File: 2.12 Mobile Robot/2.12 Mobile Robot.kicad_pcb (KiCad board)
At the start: 4 copper layers, 176 x 56 mm, 82 parts, among them J1 Motor Control B, J10 Encoder 1, J11 Encoder 2, J12 Encoder 3, J13 Encoder 4, J2 Motor Control A, J3 GND, J4 Motor Power A, J5 Battery Power, J6 Motor Power B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

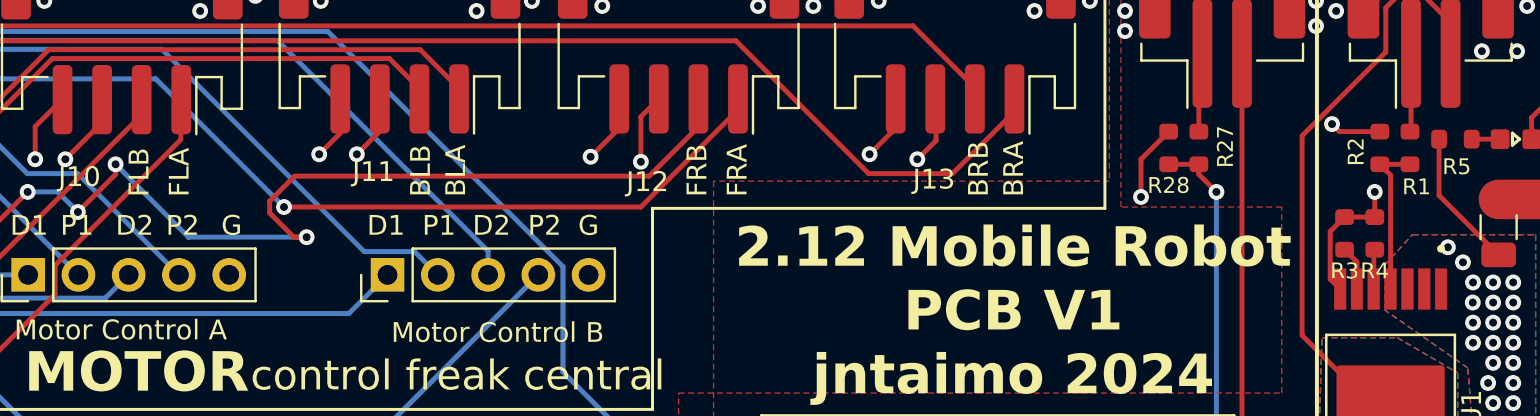
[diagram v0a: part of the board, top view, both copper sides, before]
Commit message: fixed silkscreen error
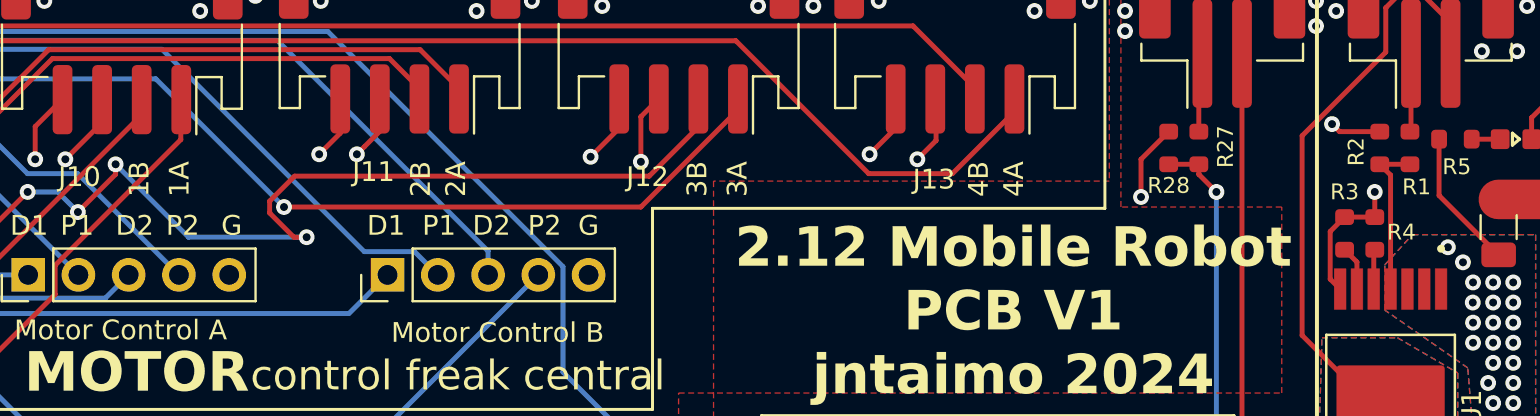
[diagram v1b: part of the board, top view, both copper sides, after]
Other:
- board text added: "1A"
- board text added: "1B"
- board text added: "2A"
- board text added: "2B"
- board text added: "3A"
- board text added: "3B"
- board text added: "4A"
- board text added: "4B"
- board text removed: "BLA"
- board text removed: "BLB"
- board text removed: "BRA"
- board text removed: "BRB"
- board text removed: "FLA"
- board text removed: "FLB"
- board text removed: "FRA"
- board text removed: "FRB"
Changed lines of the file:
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@@
   (title_block
     (title "2.12 Mobile Robot PCB")
-    (date "2024-02-17")
+    (date "2024-02-24")
     (rev "V1")
     (company "MIT jntaimo")
@@
     (property "ki_description" "1% 1 10W Thick Film Resistors 75V   100ppm    -55    155   15k   0603 Chip Resistor - Surface Mount ROHS")
     (attr smd)
-    (fp_text reference "R3" (at -1.9 0 180) (layer "F.SilkS")
+    (fp_text reference "R3" (at 2.095 0 180) (layer "F.SilkS")
         (effects (font (size 0.8 0.8) (thickness 0.15)))
     )
@@
     (property "ki_keywords" "connector")
     (attr smd)
-    (fp_text reference "J12" (at 1.572 -7.041) (layer "F.SilkS")
+    (fp_text reference "J12" (at 1.572 -6.787) (layer "F.SilkS")
         (effects (font (size 1 1) (thickness 0.15)))
     )
@@
     (property "ki_description" "1% 1 10W Thick Film Resistors 75V   100ppm    -55    155   15k   0603 Chip Resistor - Surface Mount ROHS")
     (attr smd)
-    (fp_text reference "R4" (at -1.9 0 180) (layer "F.SilkS")
+    (fp_text reference "R4" (at 0.063 1.35 180) (layer "F.SilkS")
         (effects (font (size 0.8 0.8) (thickness 0.15)))
     )
@@
     (effects (font (size 1 1) (thickness 0.15)) (justify left bottom))
   )
-  (gr_text "FRA" (at 132.08 104.902 90) (layer "F.SilkS")
+  (gr_text "3A" (at 132.08 104.902 90) (layer "F.SilkS")
     (effects (font (size 1 1) (thickness 0.15)) (justify left bottom))
   )
@@
     (effects (font (size 1 1) (thickness 0.15)) (justify left bottom))
   )
-  (gr_text "BLB" (at 116.078 104.902 90) (layer "F.SilkS")
+  (gr_text "2B" (at 116.078 104.902 90) (layer "F.SilkS")
     (effects (font (size 1 1) (thickness 0.15)) (justify left bottom))
   )
@@
     (effects (font (size 2 2) (thickness 0.4) bold) (justify left bottom))
   )
-  (gr_text "BLA" (at 117.856 104.902 90) (layer "F.SilkS")
+  (gr_text "2A" (at 117.856 104.902 90) (layer "F.SilkS")
     (effects (font (size 1 1) (thickness 0.15)) (justify left bottom))
   )
-  (gr_text "FLB" (at 101.854 104.902 90) (layer "F.SilkS")
+  (gr_text "1B" (at 101.854 104.902 90) (layer "F.SilkS")
     (effects (font (size 1 1) (thickness 0.15)) (justify left bottom))
   )
@@
     (effects (font (size 1 1) (thickness 0.15)) (justify left bottom))
   )
-  (gr_text "BRB" (at 144.272 104.902 90) (layer "F.SilkS")
+  (gr_text "4B" (at 144.272 104.902 90) (layer "F.SilkS")
     (effects (font (size 1 1) (thickness 0.15)) (justify left bottom))
   )
@@
     (effects (font (size 2 2) (thickness 0.25)) (justify bottom))
   )
-  (gr_text "FRB" (at 130.048 104.902 90) (layer "F.SilkS")
+  (gr_text "3B" (at 130.048 104.902 90) (layer "F.SilkS")
     (effects (font (size 1 1) (thickness 0.15)) (justify left bottom))
   )
@@
     )
   )
-  (gr_text "BRA" (at 146.05 104.902 90) (layer "F.SilkS")
+  (gr_text "4A" (at 146.05 104.902 90) (layer "F.SilkS")
     (effects (font (size 1 1) (thickness 0.15)) (justify left bottom))
   )
-  (gr_text "FLA" (at 103.886 104.902 90) (layer "F.SilkS")
+  (gr_text "1A" (at 103.886 104.902 90) (layer "F.SilkS")
     (effects (font (size 1 1) (thickness 0.15)) (justify left bottom))
   )
@@
   )
   (zone (net 24) (net_name "/VBAT_MOTOR") (layers "F.Cu" "In1.Cu" "In2.Cu" "B.Cu") (hatch edge 0.5)
-    (priority 2)
+    (priority 7)
     (connect_pads yes (clearance 0.5))
     (min_thickness 0.25) (filled_areas_thickness no)
